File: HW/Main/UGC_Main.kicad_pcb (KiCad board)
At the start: 4 copper layers, 125.7 x 76.4 mm, 133 parts, among them J1 Rumble, J10 Conn_01x01_Pin, J11 Conn_01x01_Pin, J12 Conn_01x01_Pin, J13 503480-0640, J14 USB4105-GF-A-060, J2 LT, J3 RT, J4 Conn_01x06_Pin, J5 Conn_01x01_Pin, J6 Conn_01x01_Pin, J7 Conn_01x01_Pin, J8 Conn_01x01_Pin, J9 Conn_01x01_Pin, Q1 MMBT3904, Q2 MMBT3904, Q3 BSS138DW, Q4 BSS138DW, Q5 Q_NMOS_GSD, Q6 Q_PMOS_GDS, Q7 Q_NMOS_GSD, SW1 SW_Push, SW10 SW_Push, SW11 SW_Push, SW12 SW_Push, SW13 SW_Push, SW14 TS09-63-25-R-260-SMT, SW2 SW_Push, SW3 SW_Push, SW4 SW_Push, SW5 SW_Push, SW6 GL18_SW, SW7 SW_Push, SW8 SW_Push, SW9 TS09-63-25-R-260-SMT, U1 ESP32-PICO-MINI-02, U10 ST_LSM6, U11 BQ25180, U12 CH340K, U13 PI3USB4000A, U2 GH39F (Hall SOT23), U3 GH39F (Hall SOT23), U4 XC6222, U5 ST_LSM6, U6 MCP3002, U7 MCP3002, U8 RP2040, U9 GD25Q80EEIGR, Y1 Crystal_GND3

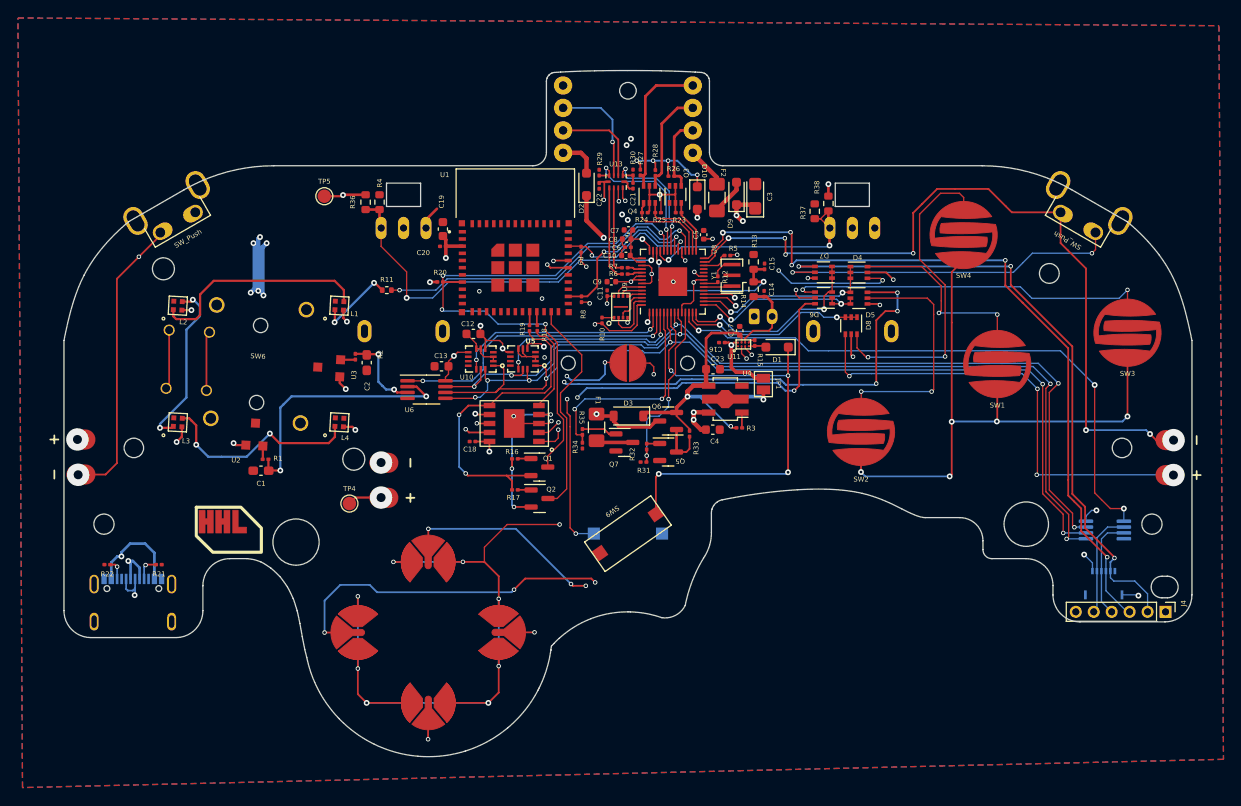
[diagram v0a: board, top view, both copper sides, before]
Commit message: Power update
- Update regulator
- Add relevant components
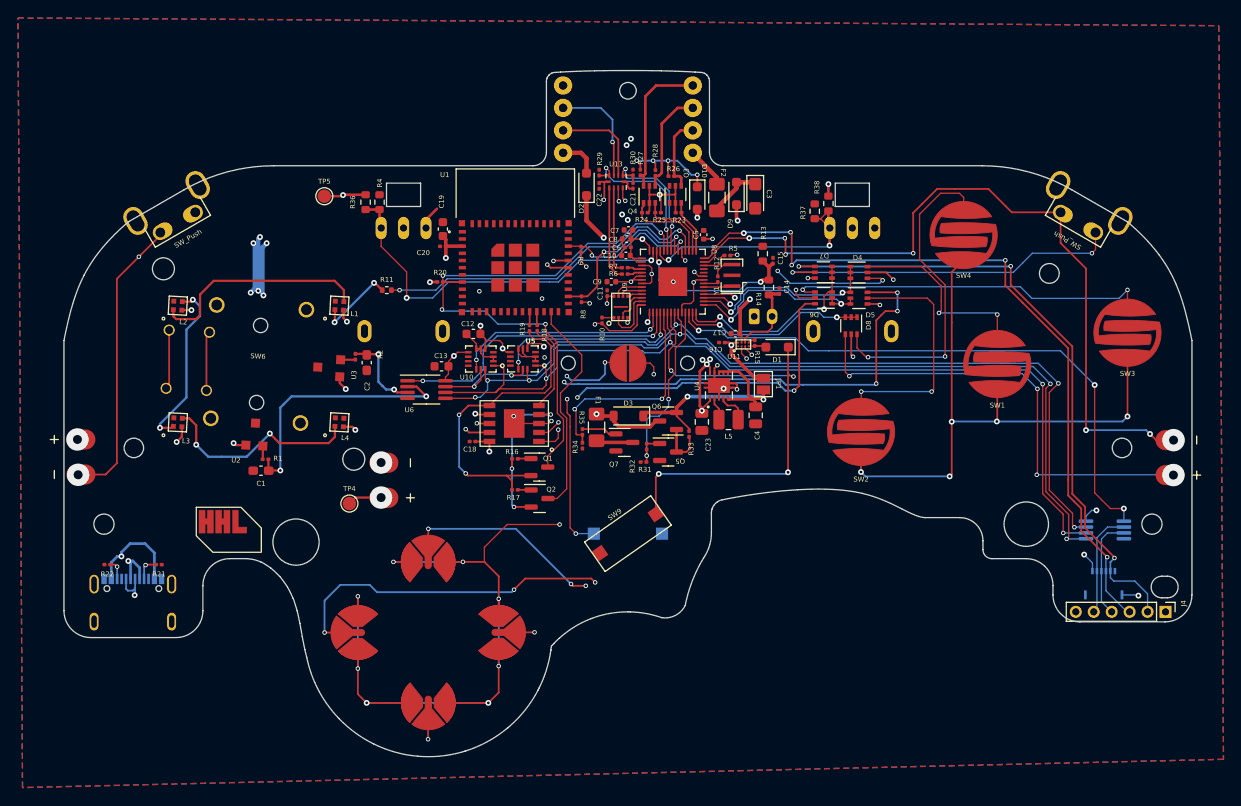
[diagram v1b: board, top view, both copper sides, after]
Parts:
- removed R3: 10k, Resistor_SMD:R_0201_0603Metric
- added L5: 1.3A 2.2uH ±20% 80mΩ, Inductor_SMD:L_1008_2520Metric, F.Cu at (229.7, 122.8)
- C23, C4: value 2.2uF -> 10uF; footprint Capacitor_SMD:C_0603_1608Metric -> Capacitor_SMD:C_0805_2012Metric
- U4: value XC6222 -> TPS630001RCR; footprint hhl:SOT-89-5 -> hhl:VREG_V62_16624-01YE
- moved C23 6.00 mm to (226.7, 123.0), turned to -90 degrees
- moved C4 5.04 mm to (232.7, 122.3), turned to 90 degrees
- moved C14 1.73 mm to (235.4, 108.5)
- moved R14 1.71 mm to (234.2, 108.1)
- moved U4 1.68 mm to (228.6, 119.0), turned to 90 degrees
- moved R13 1.37 mm to (233.5, 104.3)
- moved C15 1.13 mm to (234.6, 105.1)
- moved C17 0.58 mm to (230.5, 113.2), turned to 0 degrees
- moved R33 0.06 mm to (225.3, 124.4)
- turned C3 to -90 degrees
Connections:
- net +5V renamed VBUS
- C23 pad 1: GND -> +3V3
- C23 pad 2: VBUS_SYS -> GND
- C3 pad 1: +3V3 -> Net-(D9-A)
- C4 pad 1: +3V3 -> GND
- C4 pad 2: GND -> VBUS_SYS
- D9 pad 1: +3V3 -> VBUS_SYS
- U4 pad 1: Net-(U4-CE) -> +3V3
- U4 pad 2: GND -> Net-(U4-L2)
- U4 pad 3: unconnected-(U4-NC-Pad3) -> GND
- U4 pad 4: VBUS_SYS -> Net-(U4-L1)
- U4 pad 5: +3V3 -> VBUS_SYS
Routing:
- net VBUS_SYS: track 83.0 -> 103.0 mm, vias 4 -> 5
- net GND: track 23.6 -> 32.1 mm, vias 12 -> 15
- net Plus_Pull: track 30.8 -> 35.4 mm
- net Net-(U4-L1): track 0.00 -> 3.58 mm
- net Net-(U4-L2): track 0.00 -> 2.61 mm
- net Net-(D9-A): track 4.10 -> 6.27 mm
- net Net-(U4-CE): track 1.71 -> 0.00 mm
- net Pulldown_D: track 182.3 -> 183.9 mm
- net Scan_B: track 20.5 -> 22.1 mm
- net BTN_PWR: track 53.4 -> 54.8 mm
- net Scan_A: track 20.6 -> 21.9 mm
- net +3V3: track 116.2 -> 117.1 mm
- net VBUS: track 38.4 -> 37.5 mm

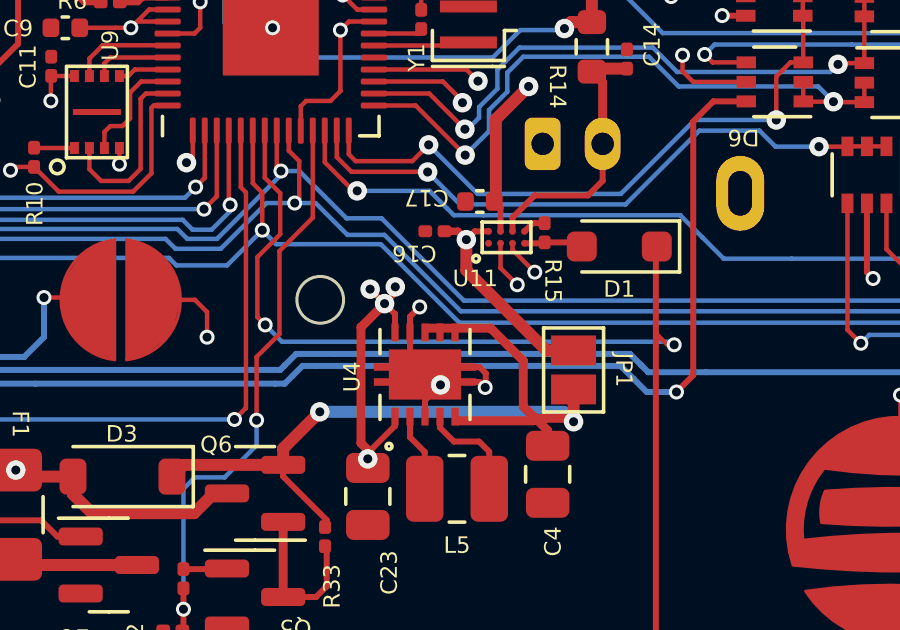
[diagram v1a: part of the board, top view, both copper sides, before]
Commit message: Update
- Remove 3d files
- Update power regulator and schematic
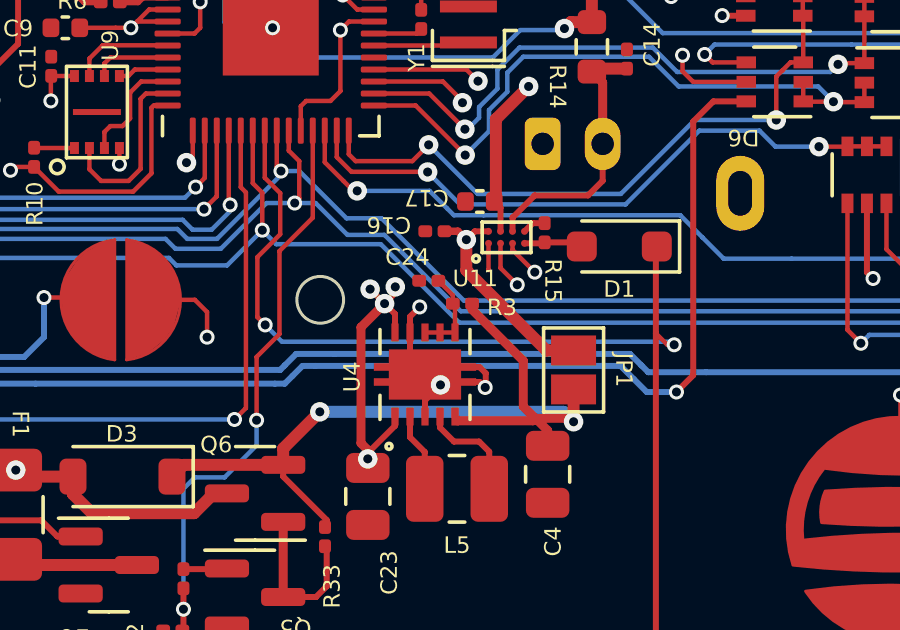
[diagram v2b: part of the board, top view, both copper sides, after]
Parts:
- added C24: 100n, Capacitor_SMD:C_0201_0603Metric, F.Cu at (228.8, 115.8)
- added R3: 100, Resistor_SMD:R_0201_0603Metric, F.Cu at (229.9, 116.6)
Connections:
- U4 pad 6: VBUS_SYS -> Net-(U4-EN)
- U4 pad 7: VBUS_SYS -> Net-(U4-EN)
- U4 pad 8: VBUS_SYS -> Net-(U4-EN)
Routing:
- net Net-(U4-EN): track 0.00 -> 2.95 mm
- net VBUS_SYS: track 103.0 -> 102.0 mm
- net unconnected-(U11-/INT-PadA1): track 0.00 -> 0.90 mm

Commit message: Firmware test
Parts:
- moved C11 0.37 mm to (215.8, 108.5), turned to 180 degrees
- moved C9 0.24 mm to (216.9, 107.5)
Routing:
- net GND: track 32.1 -> 40.4 mm, vias 15 -> 19
- net +3V3: track 117.1 -> 117.9 mm
